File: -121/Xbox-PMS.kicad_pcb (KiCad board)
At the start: 4 copper layers, 151.7 x 39.8 mm, 142 parts, among them IC1 SIC437BED-T1-GE3, IC2 SIC437BED-T1-GE3, IC3 SIC437BED-T1-GE3, IC4 SIC437BED-T1-GE3, J2 USB_C_Receptacle_USB2.0_16P, J3 Jack-DC, J6 Conn_01x04_Pin, J7 Conn_01x04_Pin, J8 Conn_01x01_Pin, J9 Conn_01x01_Pin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

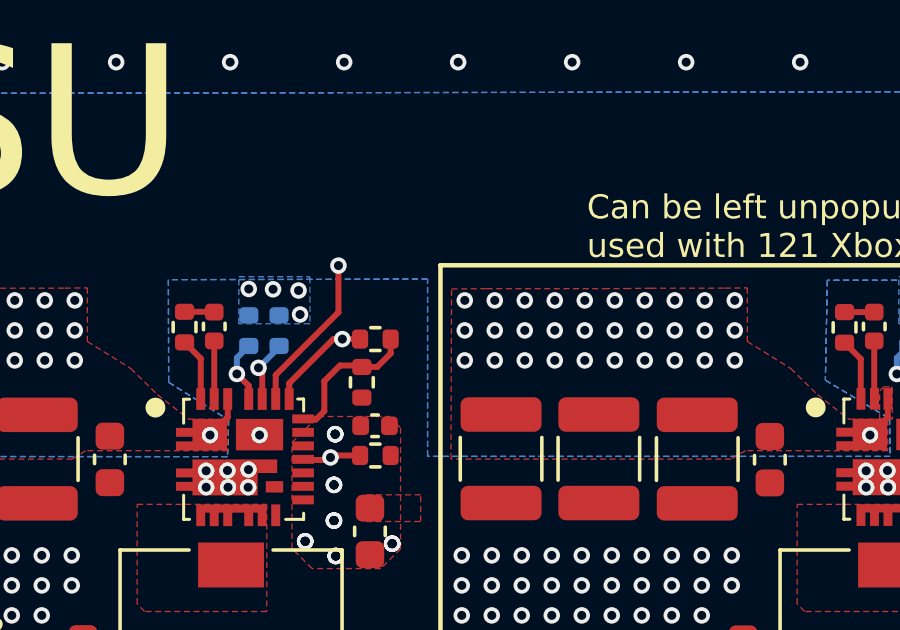
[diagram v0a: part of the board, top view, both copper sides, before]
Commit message: Add jumper 0ohm
configurable STANDBY voltage.
update silkscreen
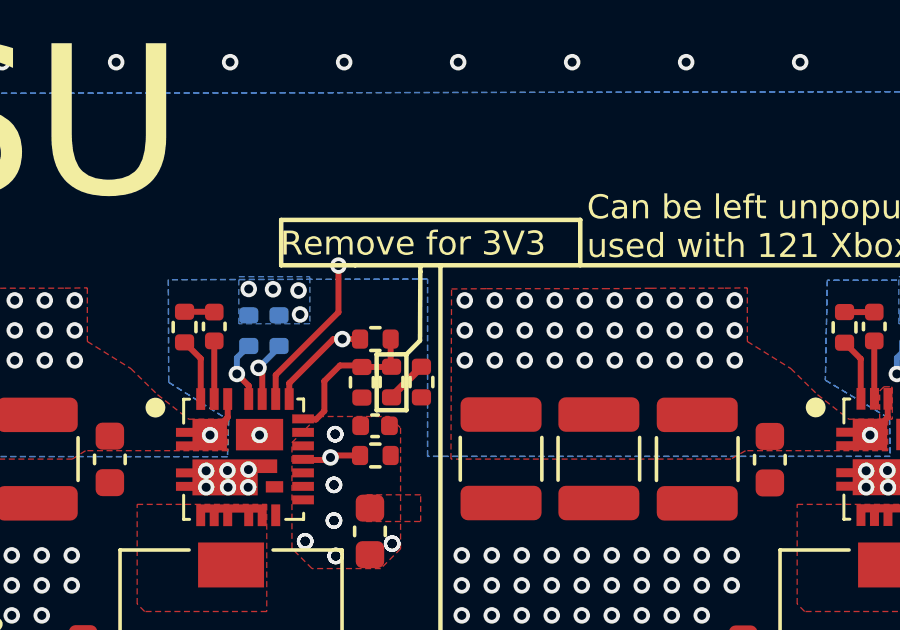
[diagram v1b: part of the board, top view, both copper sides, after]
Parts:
- added R35: 6.8K, Resistor_SMD:R_0402_1005Metric, F.Cu at (103.2, 73.2)
- added R36: 0, Resistor_SMD:R_0402_1005Metric, F.Cu at (102.2, 73.2)
- R15, R18: value 2.55K -> 4.12K
- R17: value 45K -> 18.7K
- R30: value 10K -> 430R
- R32: value 190K -> 8.2K
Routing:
- net Net-(R35-Pad1): track 0.00 -> 1.43 mm
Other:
- board text added: "Remove for 3V3"
